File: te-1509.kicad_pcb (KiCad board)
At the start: 2 copper layers, 46.6 x 29.2 mm, 8 parts, among them CN1 ce-connector, SW1 SP3T, U1 IS64WV1024, U2 CD4085

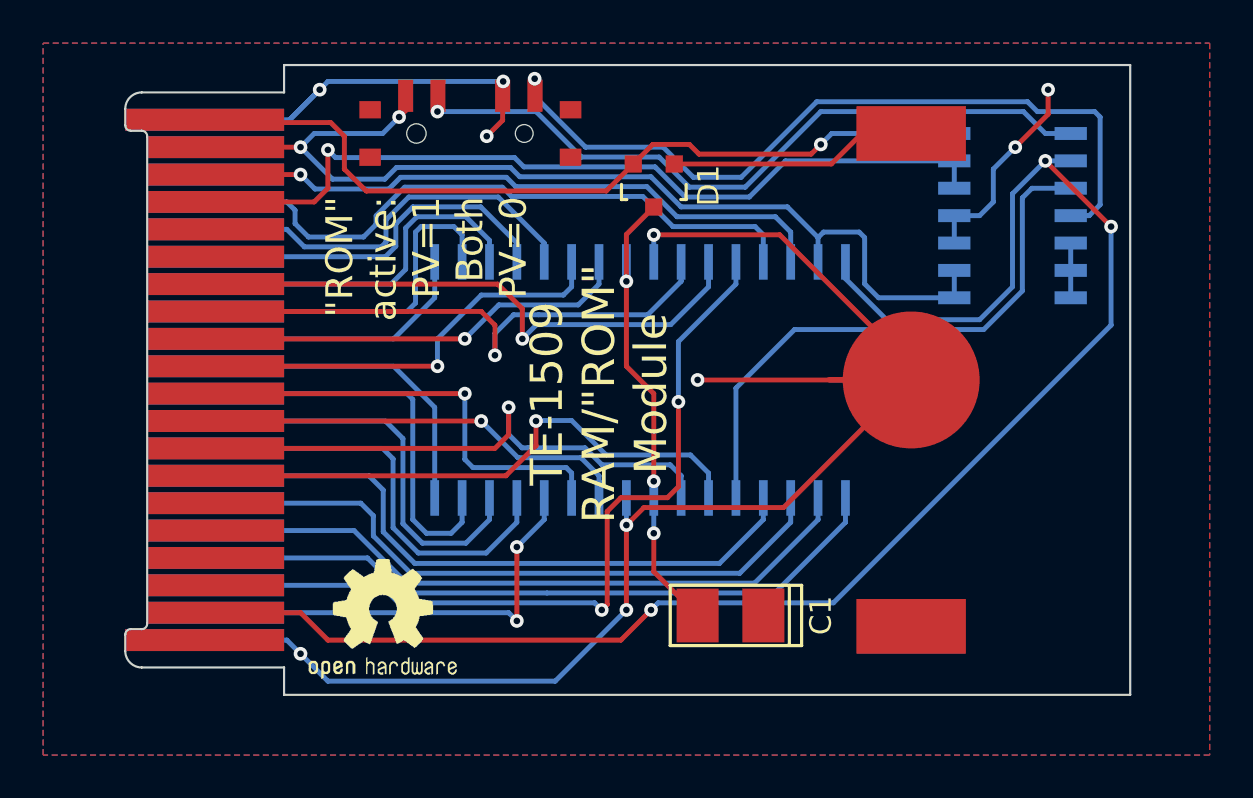
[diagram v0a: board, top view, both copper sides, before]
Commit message: Completely rework with a 5V compatible SRAM (D'oh!).
Not to mention correct active-low select logic.
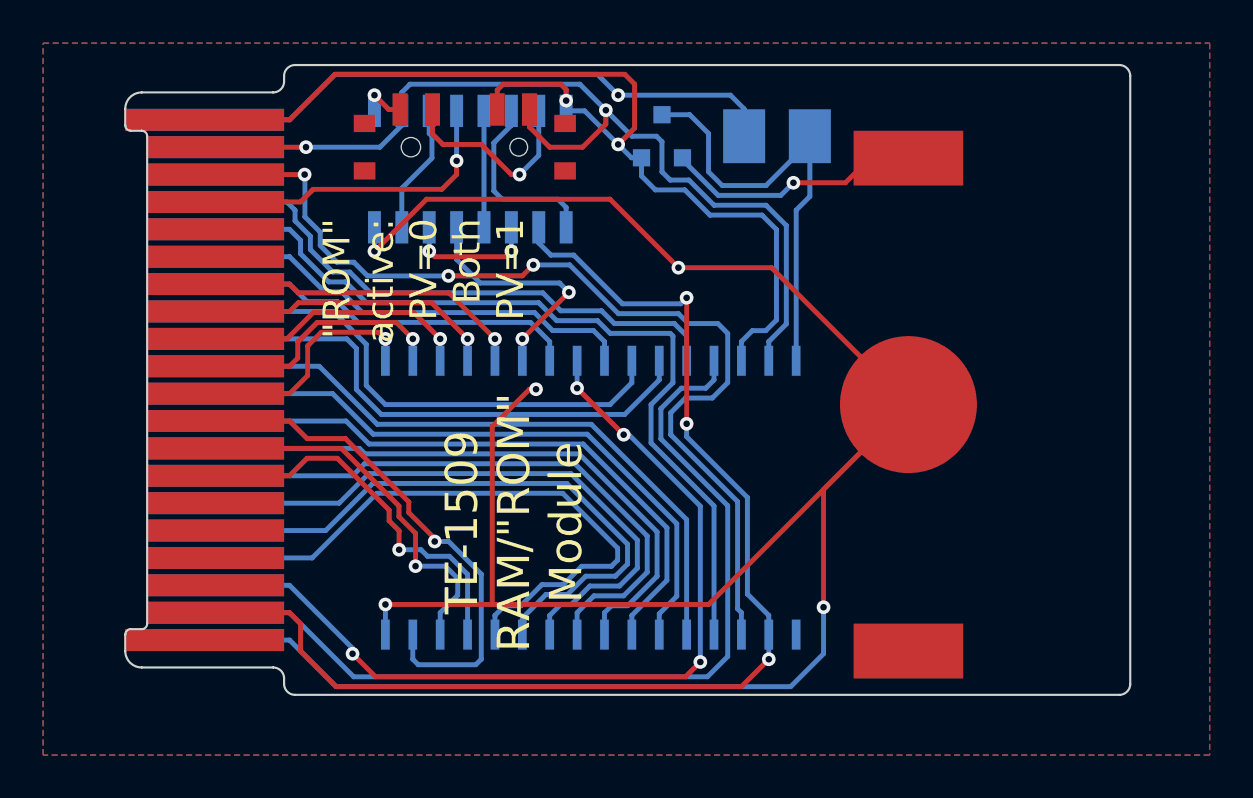
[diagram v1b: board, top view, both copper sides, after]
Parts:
- removed OSHW_LOGO: LOGO, te-1509:OSHWLOGO0.3IN
- added G***: LOGO, te-1509:OSHW_LOGO, B.Cu at (88.3, 33.8)
- C1: footprint TantalC_SizeT_EIA-3528 -> te-1509:TantalC_SizeT_EIA-3528; moved to B.Cu
- D1: moved to B.Cu
- U1: value IS64WV1024 -> AS6C1008; footprint te-1509:TSOP_II_32 -> te-1509:SOP32
- U2: value CD4085 -> CD4572; footprint Housings_SOIC:SOIC-14_3.9x8.7mm_Pitch1.27mm -> Housings_SOIC:SOIC-16_3.9x9.9mm_Pitch1.27mm
- moved U2 25.2 mm to (64.0, 24.0), turned to 90 degrees
- moved C1 22.3 mm to (78.2, 22.5)
- moved U1 5.92 mm to (69.6, 39.2)
- moved D1 2.32 mm to (72.9, 22.5)
- moved BT1 1.15 mm to (84.3, 34.9)
- moved SW1 0.68 mm to (63.8, 23.0)
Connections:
- C1 pad 1: GND -> /VRR
- C1 pad 2: /VRR -> GND
- SW1 pad 1: /BANK8 -> /BSW
- SW1 pad 2: /~PV -> /PV
- SW1 pad 3: GND -> VCC
- SW1 pad 4: /PV -> /~PV
- U1 pad 1: /AD0 -> (no net)
- U1 pad 10: /D2 -> /AD2
- U1 pad 11: /D3 -> /AD1
- U1 pad 12: /~WE -> /AD0
- U1 pad 13: /AD4 -> /D0
- U1 pad 14: /AD5 -> /D1
- U1 pad 15: /AD6 -> /D2
- U1 pad 16: /AD7 -> GND
- U1 pad 17: /AD8 -> /D3
- U1 pad 18: /AD9 -> /D4
- U1 pad 19: /AD10 -> /D5
- U1 pad 2: /AD1 -> /~Y2
- U1 pad 20: /AD11 -> /D6
- U1 pad 21: /AD12 -> /D7
- U1 pad 22: /D4 -> /~CE
- U1 pad 23: /D5 -> /AD10
- U1 pad 24: /VRR -> /~OD
- U1 pad 25: GND -> /AD11
- U1 pad 26: /D6 -> /AD9
- U1 pad 27: /D7 -> /AD8
- U1 pad 28: /~OD -> /AD13
- U1 pad 29: /AD13 -> /~WE
- U1 pad 3: /AD2 -> /PU
- U1 pad 30: /PU -> VCC
- U1 pad 32: /~Y2 -> /VRR
- U1 pad 4: /AD3 -> /AD12
- U1 pad 5: /~CE -> /AD7
- U1 pad 6: /D0 -> /AD6
- U1 pad 7: /D1 -> /AD5
- U1 pad 8: /VRR -> /AD4
- U1 pad 9: GND -> /AD3
- U2 pad 1: /BANK8 -> /Y2
- U2 pad 10: GND -> /PV
- U2 pad 11: GND -> /Y0
- U2 pad 13: /~Y0 -> Net-(U2-Pad13)
- U2 pad 14: VCC -> /Y2
- U2 pad 3: /~CE -> Net-(U2-Pad3)
- U2 pad 4: /~PV -> Net-(U2-Pad13)
- U2 pad 5: GND -> /~CE
- U2 pad 6: GND -> Net-(U2-Pad3)
- U2 pad 7: GND -> /Y0
- U2 pad 8: /PV -> GND
- U2 pad 9: /PV -> /~PV
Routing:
- net GND: track 106.1 -> 142.6 mm, vias 10 -> 6
- net /~PV: track 37.4 -> 2.19 mm
- net /BANK8: track 34.1 -> 0.00 mm, vias 1 -> 0
- net /~Y0: track 39.2 -> 14.7 mm
- net /~WE: track 20.4 -> 42.1 mm, vias 2 -> 0
- net /AD12: track 18.9 -> 39.1 mm
- net /~Y2: track 74.6 -> 55.6 mm
- net /PU: track 29.6 -> 45.9 mm, vias 1 -> 3
- net /~CE: track 27.0 -> 11.4 mm, vias 0 -> 2
- net /AD7: track 15.2 -> 30.1 mm
- net /D6: track 26.2 -> 13.6 mm
- net /AD8: track 12.6 -> 24.7 mm
- net /D7: track 26.9 -> 15.0 mm
- net VCC: track 38.5 -> 49.5 mm, vias 1 -> 2
- net /AD6: track 18.7 -> 29.4 mm
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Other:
- outline, holes or cut-outs redrawn
- board text added: ""ROM" active: PV=0 Both PV=1"
- board text removed: ""ROM" active: PV=1 Both PV=0"

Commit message: routing tweaks
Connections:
- net Net-(U2-Pad13) renamed /~RE
- net Net-(U2-Pad3) renamed /RE
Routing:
- net GND: track 142.6 -> 117.5 mm
- net /AD0: track 29.1 -> 18.9 mm
- net /AD1: track 28.8 -> 19.3 mm
- net /AD2: track 28.6 -> 20.9 mm
- net /AD3: track 28.4 -> 21.2 mm
- net /AD4: track 28.3 -> 22.5 mm
- net /AD5: track 28.6 -> 24.3 mm
- net /AD6: track 29.4 -> 26.5 mm
- net /AD7: track 30.1 -> 28.6 mm
- net /Y0: track 6.03 -> 6.79 mm
- net /PU: track 45.9 -> 45.3 mm

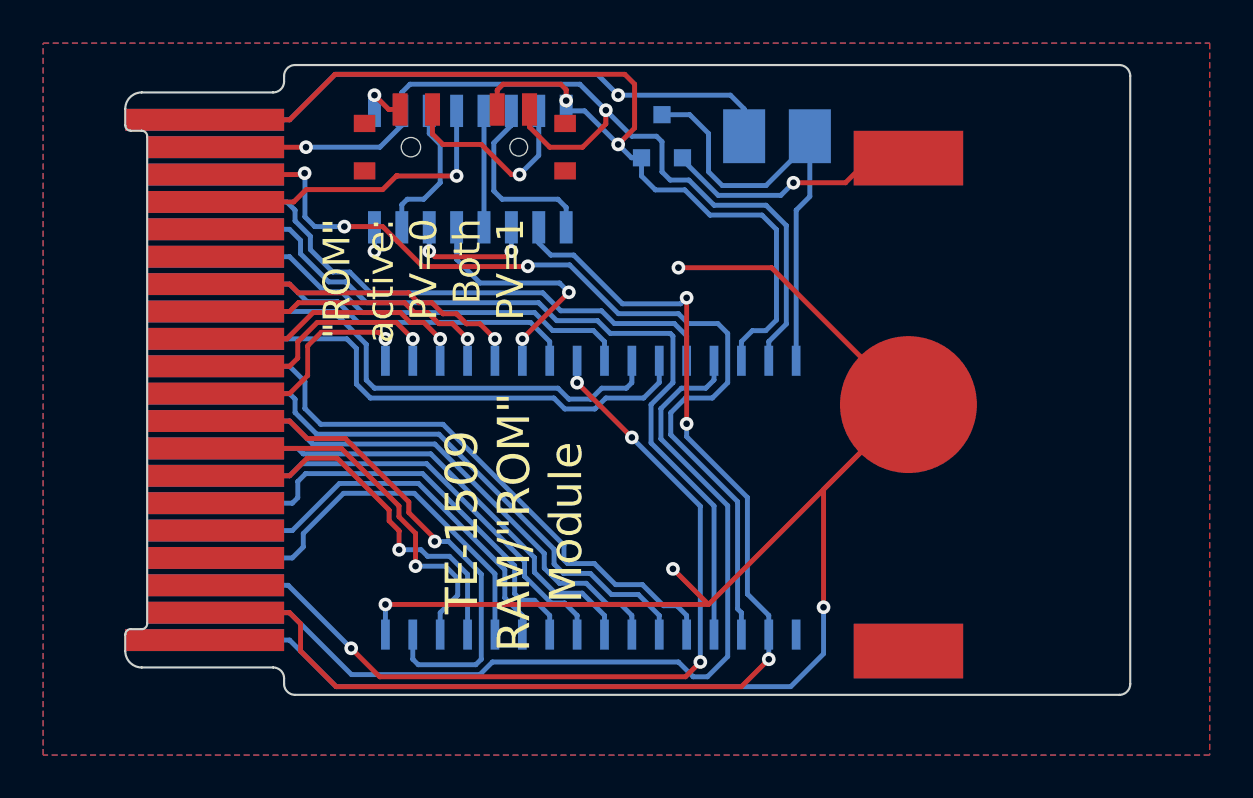
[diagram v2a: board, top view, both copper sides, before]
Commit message: switch to aluminum capacitor
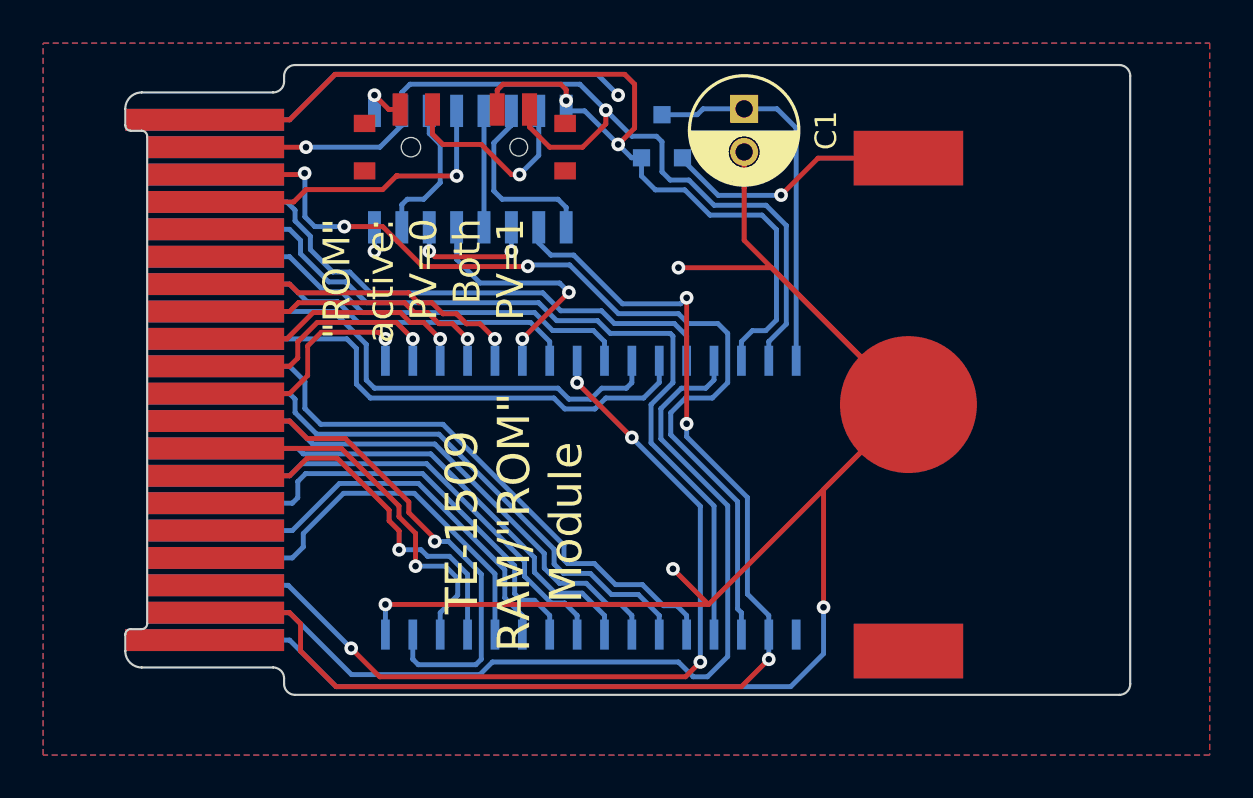
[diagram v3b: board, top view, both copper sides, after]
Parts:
- C1: value 220u -> 100u; footprint te-1509:TantalC_SizeT_EIA-3528 -> Capacitors_ThroughHole:C_Radial_D5_L11_P2; moved to F.Cu
- moved C1 1.98 mm to (76.7, 21.2), turned to 270 degrees
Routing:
- net GND: track 117.5 -> 125.0 mm
- net /VRR: track 21.0 -> 17.5 mm
- net /BT+: track 12.0 -> 13.7 mm

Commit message: switch to thinner cr2016, back to tantalum cap(s)
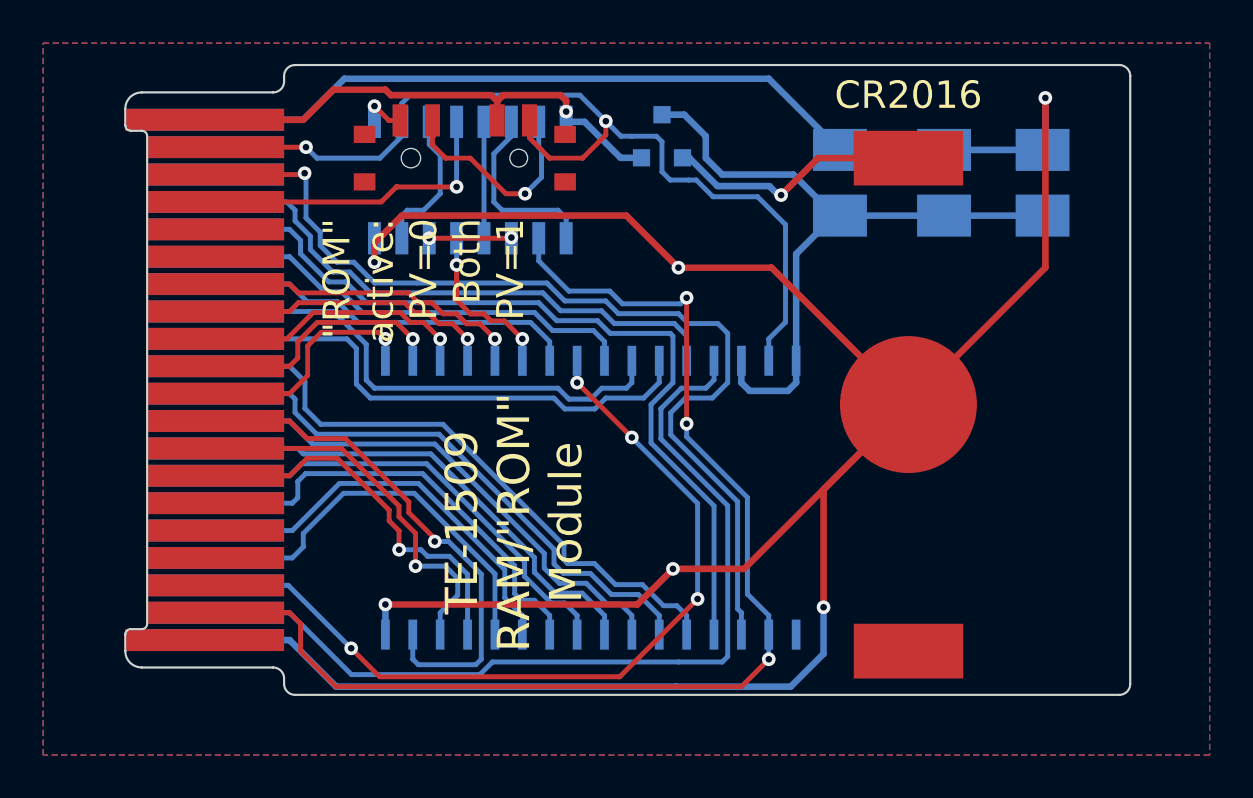
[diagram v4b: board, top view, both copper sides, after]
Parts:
- added C2: 33u, te-1509:TantalC_SizeT_EIA-3528, B.Cu at (86.0, 24.6)
- added C3: 33u, te-1509:TantalC_SizeT_EIA-3528, B.Cu at (90.6, 24.6)
- BT1: footprint te-1509:CR2032 -> te-1509:Coin_20mm
- C1: value 100u -> 33u; footprint Capacitors_ThroughHole:C_Radial_D5_L11_P2 -> te-1509:TantalC_SizeT_EIA-3528; moved to B.Cu
- moved C1 5.61 mm to (81.2, 24.6)
- moved G*** 5.47 mm to (87.9, 39.2)
- moved SW1 0.51 mm to (63.8, 23.5)
- moved U2 0.51 mm to (64.0, 24.5)
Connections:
- U1 pad 30: VCC -> /VRR
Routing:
- net GND: track 125.0 -> 198.5 mm
- net /VRR: track 17.5 -> 43.8 mm
- net VCC: track 49.5 -> 29.5 mm, vias 2 -> 1
- net /BT+: track 13.7 -> 18.1 mm
- net /~CE: track 11.4 -> 7.67 mm
- net /RE: track 6.24 -> 3.86 mm
- net /~OD: track 40.9 -> 39.0 mm
- net /BSW: track 9.28 -> 10.1 mm
- net /~WE: track 42.5 -> 42.0 mm
- net /PU: track 45.3 -> 45.6 mm, vias 3 -> 1
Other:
- net class Power added: clearance 0.2286, trace_width 0.3048, via_dia 0.635, via_drill 0.3048
- board text added: "CR2016"

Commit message: pullup/pulldown sram enable resistors
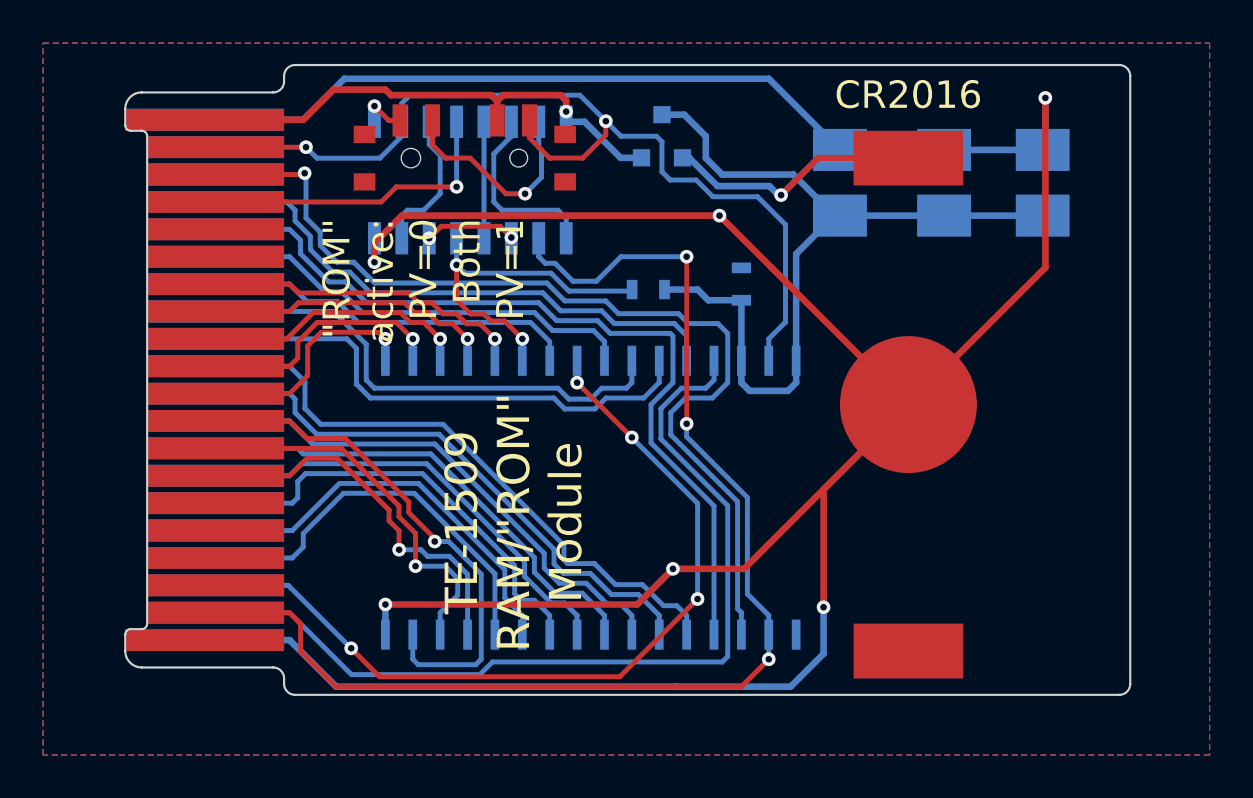
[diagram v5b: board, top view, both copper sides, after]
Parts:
- added R1: 50k, Resistors_SMD:R_0603, B.Cu at (76.6, 29.3)
- added R2: 50k, Resistors_SMD:R_0603, B.Cu at (72.3, 29.6)
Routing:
- net /~CE: track 7.67 -> 16.3 mm
- net /VRR: track 43.8 -> 50.4 mm
- net GND: track 198.5 -> 194.1 mm
- net /~Y2: track 55.5 -> 57.2 mm

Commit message: Switch to VGG as appropriate.
The VGG supply is on 100% of the time.  Keep SRAM powered from it,
saving the lithium backup.  The VCC supply switches on and off with the
power controls, so power the rest of the circuitry from that.
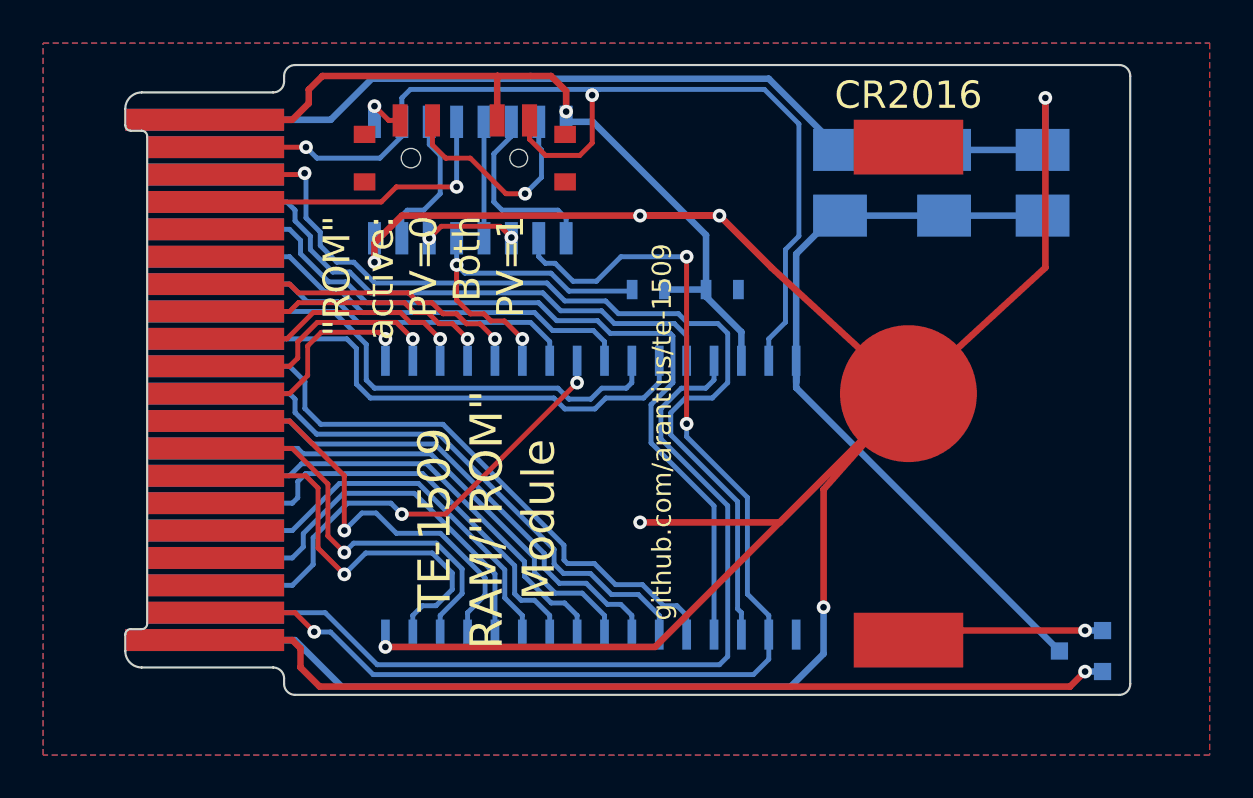
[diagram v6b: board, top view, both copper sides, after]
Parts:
- moved D1 30.8 mm to (92.3, 46.4), turned to 270 degrees
- moved G*** 3.30 mm to (87.9, 35.9)
- moved R1 0.92 mm to (75.7, 29.6), turned to 0 degrees
- moved BT1 0.51 mm to (84.3, 34.4)
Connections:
- CN1 pad 1: VCC -> /VCC
- CN1 pad 20: (no net) -> /VGG
- D1 pad 2: VCC -> /VGG
- R1 pad 1: /VRR -> /VCC
- R2 pad 1: /VRR -> /VCC
- SW1 pad 3: VCC -> /VCC
- U1 pad 13: /D0 -> /D2
- U1 pad 15: /D2 -> /D0
- U1 pad 30: /VRR -> /VCC
- U2 pad 16: VCC -> /VCC
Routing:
- net /VGG: track 0.00 -> 43.3 mm, vias 0 -> 1
- net /VCC: track 0.00 -> 38.9 mm, vias 0 -> 1
- net VCC: track 29.5 -> 0.00 mm, vias 1 -> 0
- net /~OD: track 39.0 -> 22.8 mm, vias 4 -> 2
- net /VRR: track 50.4 -> 37.4 mm
- net /BT+: track 18.0 -> 11.0 mm
- net /PV: track 44.5 -> 48.7 mm
- net /D2: track 24.1 -> 20.6 mm
- net GND: track 194.1 -> 192.4 mm, vias 6 -> 7
- net /D0: track 17.8 -> 19.3 mm
- net /~Y2: track 57.2 -> 56.0 mm
- net /D1: track 17.8 -> 19.0 mm
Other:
- board text added: "github.com/arantius/te-1509"
